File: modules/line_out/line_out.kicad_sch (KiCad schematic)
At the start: 24 parts, among them J1 AudioJack3, U1 TL072

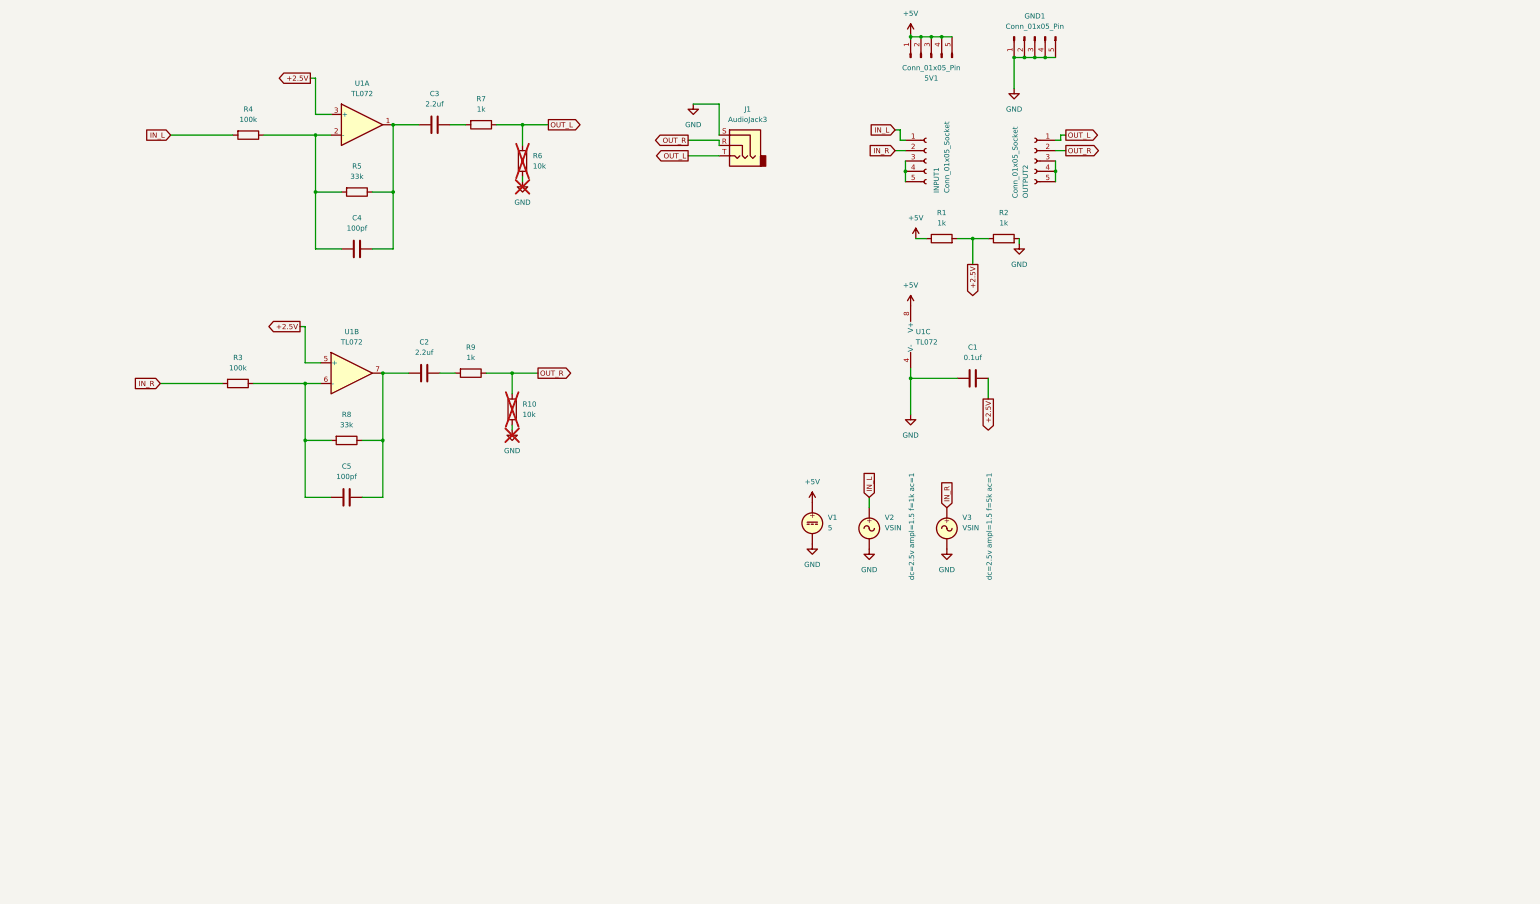
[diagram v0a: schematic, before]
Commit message: line_out: Introduce input buffering
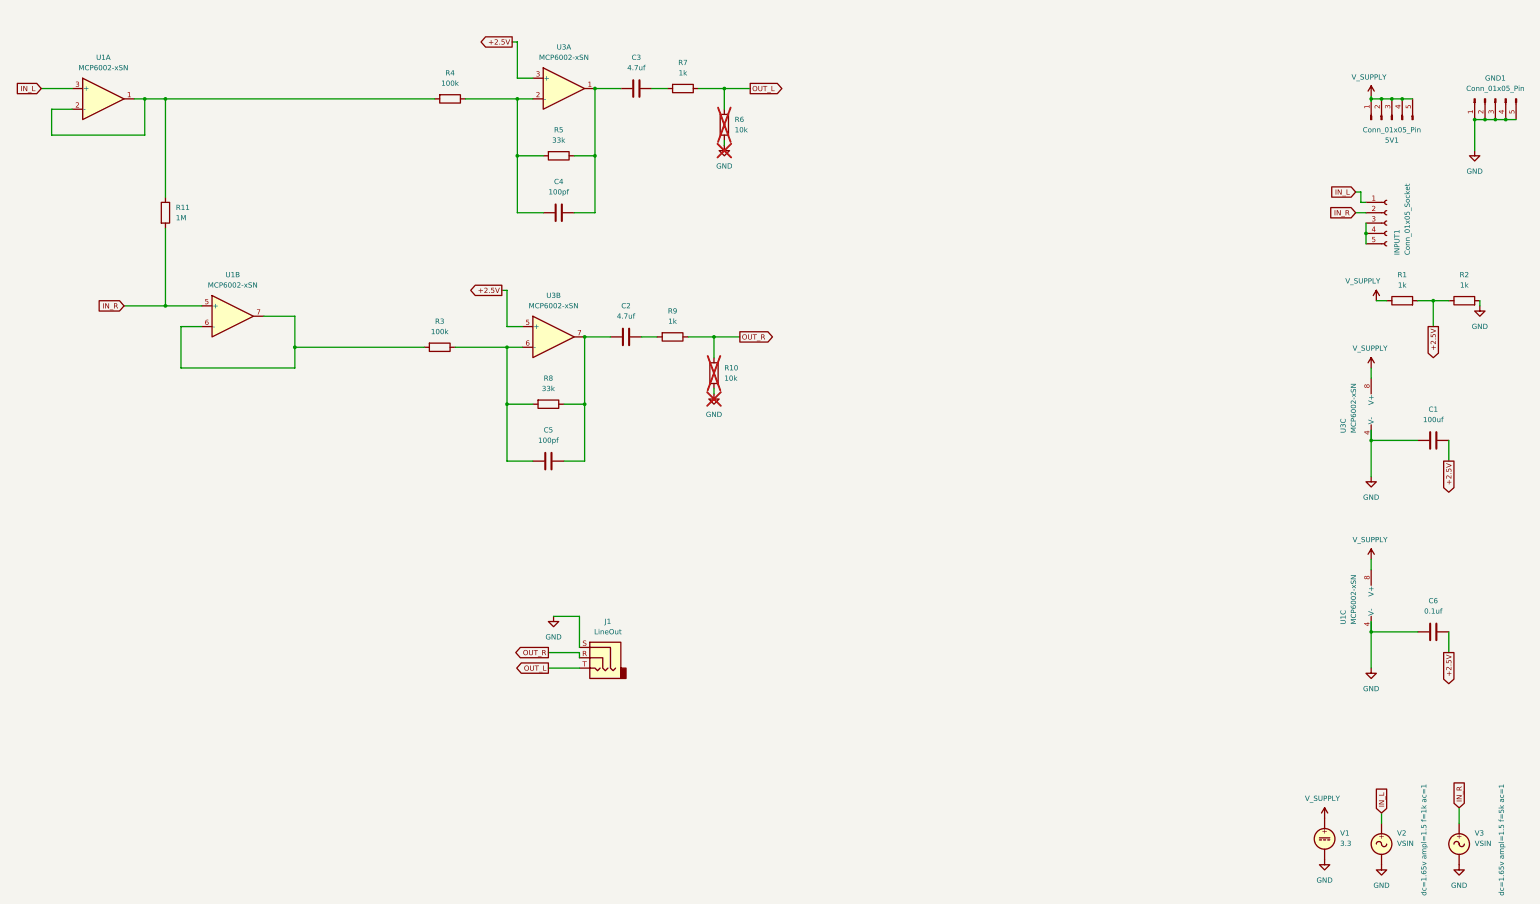
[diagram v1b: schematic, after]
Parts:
- removed OUTPUT2: Conn_01x05_Socket, Connector_PinSocket_2.54mm:PinSocket_1x05_P2.54mm_Vertical, symbol Connector:Conn_01x05_Socket
- removed U1: TL072, Package_SO:SOIC-8-1EP_3.9x4.9mm_P1.27mm_EP2.29x3mm, symbol Amplifier_Operational:TL072
- added C6: 0.1uf, Capacitor_SMD:C_0402_1005Metric, symbol Device:C
- added R11: 1M, Resistor_SMD:R_0402_1005Metric, symbol Device:R
- added U1, U3: MCP6002-xSN, Package_SO:SOIC-8-1EP_3.9x4.9mm_P1.27mm_EP2.29x3mm, symbol Amplifier_Operational:MCP6002-xSN
- C1: value 0.1uf -> 100uf; footprint Capacitor_SMD:C_0402_1005Metric -> Capacitor_SMD:C_1206_3216Metric
- C2, C3: value 2.2uf -> 4.7uf
- J1: value AudioJack3 -> LineOut
- V1: value 5 -> 3.3
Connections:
- net +2.5V: now also C6.2, U3.3 (+), U3.5 (+)
- net GND: now also C6.1, U1.4 (V-), U3.4 (V-)
- net IN_L: now also U1.3 (+); no longer R4.2
- net IN_R: now also R11.2, U1.5 (+); no longer R3.2
- net at C2.1, C5.1, R8.1: now also U3.7
- net at C3.1, C4.1, R5.1: now also U3.1
- net at C4.2, R4.1, R5.2: now also U3.2 (-)
- net at C5.2, R3.1, R8.2: now also U3.6 (-)
- net +5V renamed V_SUPPLY
- net V_SUPPLY: now also U1.8 (V+), U3.8 (V+)
- new net: R11.1, R4.2, U1.1, U1.2 (-)
- new net: R3.2, U1.6 (-), U1.7
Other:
- moved on the sheet: 5V1, C1, C2, C3, C4, C5, GND1, INPUT1, J1, R1, R10, R2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

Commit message: Remove opamp for buffering. It adds noise & hums due to use of non-inverting buffers When used inverting buffers L->R relaying has a phase shift So better not to use
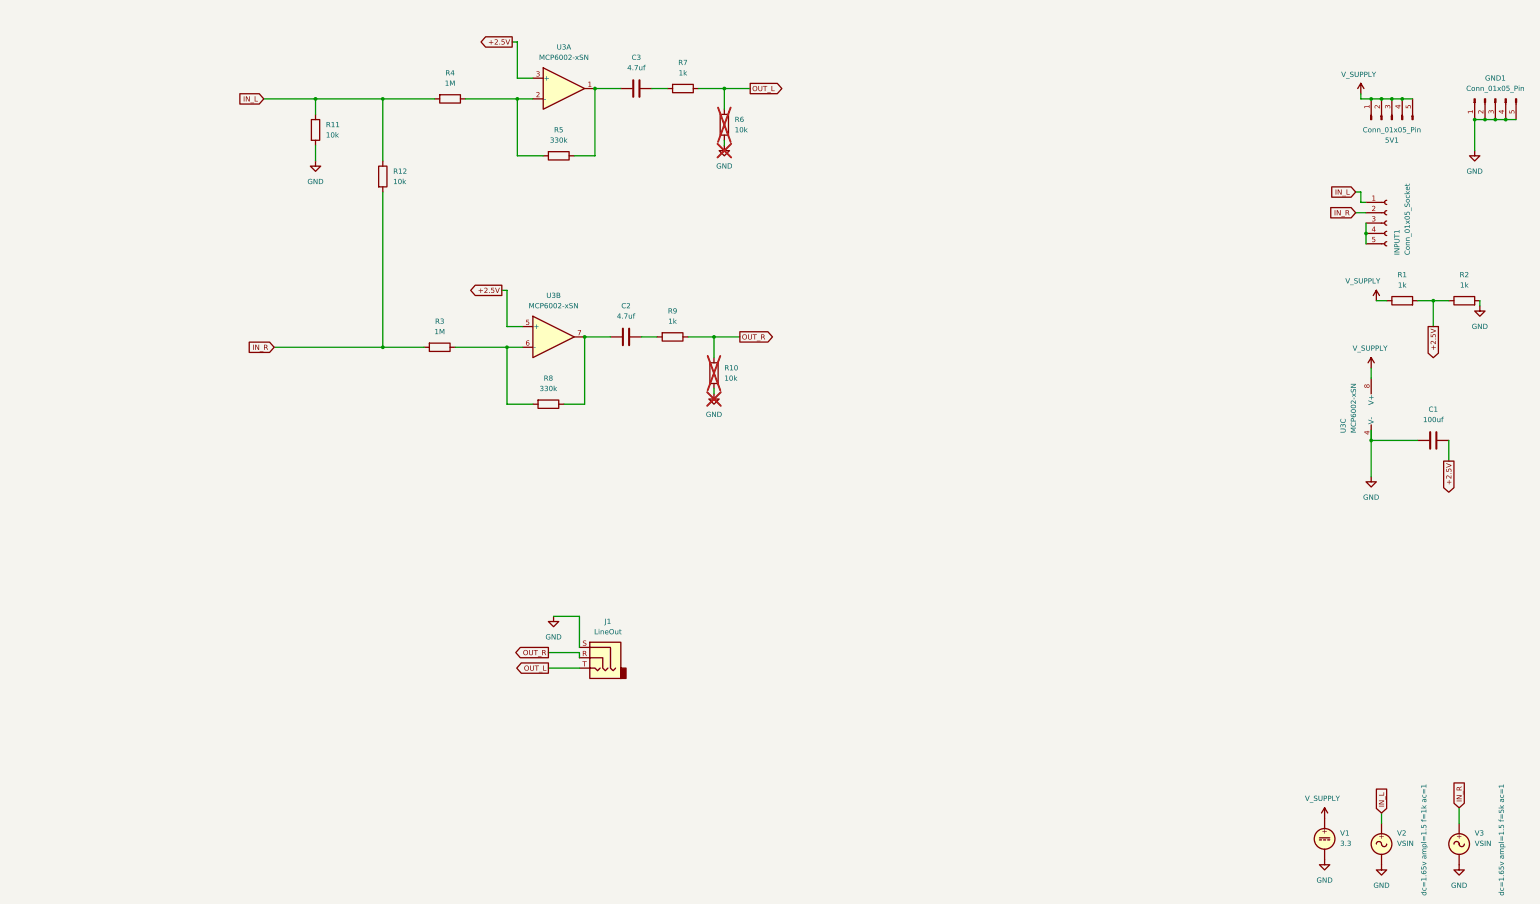
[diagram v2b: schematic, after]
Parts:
- removed C4, C5: 100pf, Capacitor_SMD:C_0402_1005Metric, symbol Device:C
- removed C6: 0.1uf, Capacitor_SMD:C_0402_1005Metric, symbol Device:C
- removed U1: MCP6002-xSN, Package_SO:SOIC-8-1EP_3.9x4.9mm_P1.27mm_EP2.29x3mm, symbol Amplifier_Operational:MCP6002-xSN
- added R12: 10k, Resistor_SMD:R_0402_1005Metric, symbol Device:R
- R11: value 1M -> 10k
- R3, R4: value 100k -> 1M
- R5, R8: value 33k -> 330k
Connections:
- net GND: now also R11.2
- net IN_L: now also R11.1, R4.2, R12.1
- net IN_R: now also R3.2, R12.2; no longer R11.2

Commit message: line_out: Update resistor footprints to match with the JLCPCB basic parts
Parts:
- R5, R8: footprint Resistor_SMD:R_0402_1005Metric -> Resistor_SMD:R_0603_1608Metric
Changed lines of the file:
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@@
 			)
 		)
-		(property "Footprint" "Resistor_SMD:R_0402_1005Metric"
+		(property "Footprint" "Resistor_SMD:R_0603_1608Metric"
 			(at 144.78 113.792 90)
 			(effects
@@
 			)
 		)
-		(property "Footprint" "Resistor_SMD:R_0402_1005Metric"
+		(property "Footprint" "Resistor_SMD:R_0603_1608Metric"
 			(at 147.32 52.832 90)
 			(effects
